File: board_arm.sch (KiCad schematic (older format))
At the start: 153 parts, among them SW1 SW_SPDT, U1 STM32F072CBT6, U2 PRTR5V0U2X, U3 MCP1725-3302E_SN

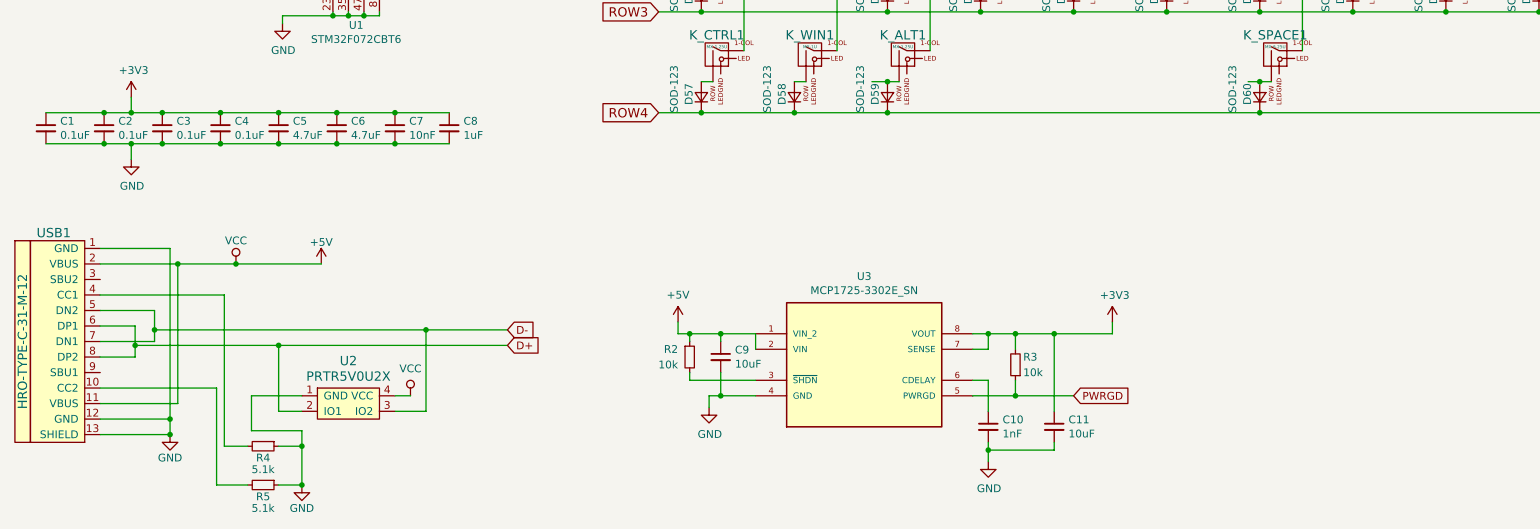
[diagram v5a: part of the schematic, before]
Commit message: basic routing of sigs and power supply
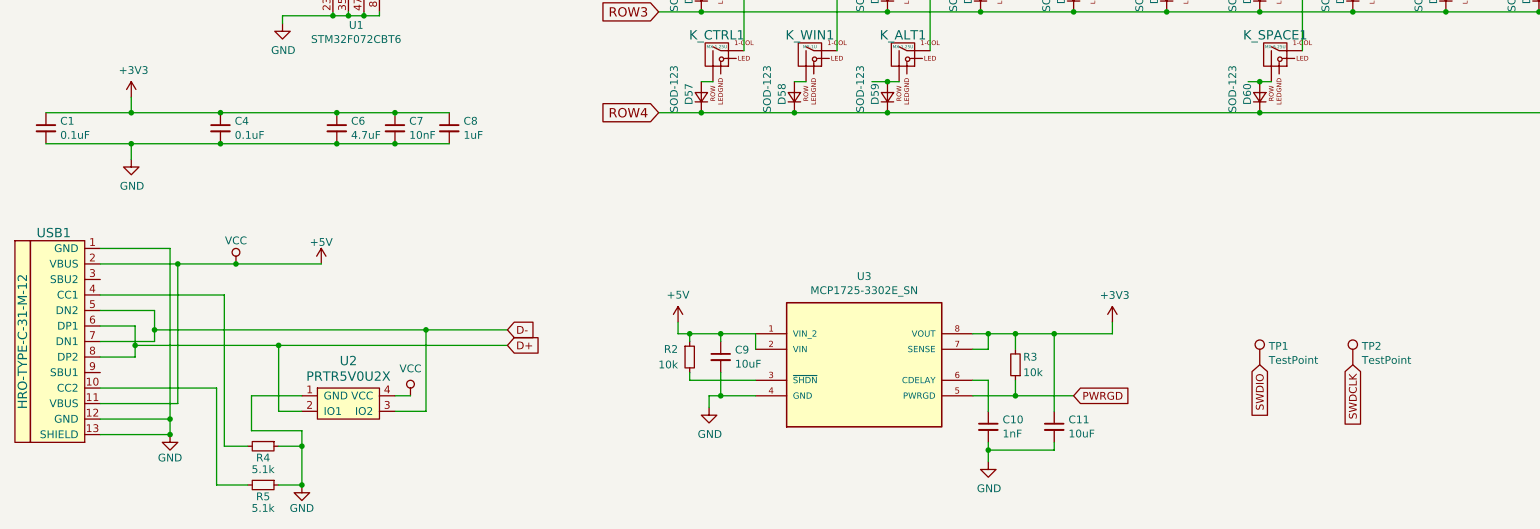
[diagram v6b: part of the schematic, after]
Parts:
- removed C2, C3: 0.1uF, Capacitor_SMD:C_0805_2012Metric, symbol Device:C_Small
- removed C5: 4.7uF, Capacitor_SMD:C_0805_2012Metric, symbol Device:C_Small
- added TP1, TP2: TestPoint, TestPoint:TestPoint_Pad_D1.0mm, symbol Connector:TestPoint
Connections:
- net SWDCLK: now also TP2.1
- net SWDIO: now also TP1.1
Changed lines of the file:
@@
-$EndComp
-$Comp
-L Device:C_Small C2
-U 1 1 5C603F7E
-P 1450 5275
-F 0 "C2" H 1542 5321 50  0000 L CNN
-F 1 "0.1uF" H 1542 5230 50  0000 L CNN
-F 2 "Capacitor_SMD:C_0805_2012Metric" H 1450 5275 50  0001 C CNN
-F 3 "~" H 1450 5275 50  0001 C CNN
-	1    1450 5275
-	1    0    0    -1
-$EndComp
-$Comp
-L Device:C_Small C3
-U 1 1 5C603FAE
-P 1825 5275
-F 0 "C3" H 1917 5321 50  0000 L CNN
-F 1 "0.1uF" H 1917 5230 50  0000 L CNN
-F 2 "Capacitor_SMD:C_0805_2012Metric" H 1825 5275 50  0001 C CNN
-F 3 "~" H 1825 5275 50  0001 C CNN
-	1    1825 5275
-	1    0    0    -1
 $EndComp
 $Comp
@@
 PWRGD
 $Comp
-L Device:C_Small C5
-U 1 1 5D260E0E
-P 2575 5275
-F 0 "C5" H 2667 5321 50  0000 L CNN
-F 1 "4.7uF" H 2667 5230 50  0000 L CNN
-F 2 "Capacitor_SMD:C_0805_2012Metric" H 2575 5275 50  0001 C CNN
-F 3 "~" H 2575 5275 50  0001 C CNN
-	1    2575 5275
-	1    0    0    -1
-$EndComp
-$Comp
 L Device:C_Small C6
 U 1 1 5D2621C9
@@
 Wire Wire Line
 	3325 1500 3500 1500
-Connection ~ 1450 5175
-Connection ~ 1450 5375
-Connection ~ 1825 5175
-Connection ~ 1825 5375
 Connection ~ 2200 5175
 Connection ~ 2200 5375
-Connection ~ 2575 5175
-Connection ~ 2575 5375
 Connection ~ 2950 5175
 Connection ~ 2950 5375
 Wire Wire Line
-	1825 5375 2200 5375
-Wire Wire Line
-	1075 5375 1450 5375
-Wire Wire Line
-	1075 5175 1450 5175
-Wire Wire Line
-	1825 5175 2200 5175
-Wire Wire Line
-	2575 5175 2950 5175
-Wire Wire Line
-	2575 5375 2950 5375
-Wire Wire Line
-	2200 5175 2575 5175
-Wire Wire Line
 	2950 5175 3325 5175
-Wire Wire Line
-	2200 5375 2575 5375
 Connection ~ 3325 5175
 Wire Wire Line
@@
 	1625 5175 1625 5075
 Connection ~ 1625 5175
-Wire Wire Line
-	1625 5175 1825 5175
-Wire Wire Line
-	1450 5175 1625 5175
 Connection ~ 1625 5375
-Wire Wire Line
-	1625 5375 1825 5375
-Wire Wire Line
-	1450 5375 1625 5375
 Wire Wire Line
 	7150 6700 7050 6700
@@
 Wire Wire Line
 	9175 2050 9175 4775
+$Comp
+L Connector:TestPoint TP1
+U 1 1 5C6EFC1B
+P 8900 6800
+F 0 "TP1" H 8958 6920 50  0000 L CNN
+F 1 "TestPoint" H 8958 6829 50  0000 L CNN
+F 2 "TestPoint:TestPoint_Pad_D1.0mm" H 9100 6800 50  0001 C CNN
+F 3 "~" H 9100 6800 50  0001 C CNN
+	1    8900 6800
+	1    0    0    -1
+$EndComp
+Text GLabel 8900 6800 3    50   Input ~ 0
+SWDIO
+Text GLabel 9500 6800 3    50   Input ~ 0
+SWDCLK
+$Comp
+L Connector:TestPoint TP2
+U 1 1 5C7259A1
+P 9500 6800
+F 0 "TP2" H 9558 6920 50  0000 L CNN
+F 1 "TestPoint" H 9558 6829 50  0000 L CNN
+F 2 "TestPoint:TestPoint_Pad_D1.0mm" H 9700 6800 50  0001 C CNN
+F 3 "~" H 9700 6800 50  0001 C CNN
+	1    9500 6800
+	1    0    0    -1
+$EndComp
+Wire Wire Line
+	1075 5175 1625 5175
+Wire Wire Line
+	1075 5375 1625 5375
+Wire Wire Line
+	1625 5175 2200 5175
+Wire Wire Line
+	1625 5375 2200 5375
+Wire Wire Line
+	2200 5175 2950 5175
+Wire Wire Line
+	2200 5375 2950 5375
 $EndSCHEMATC

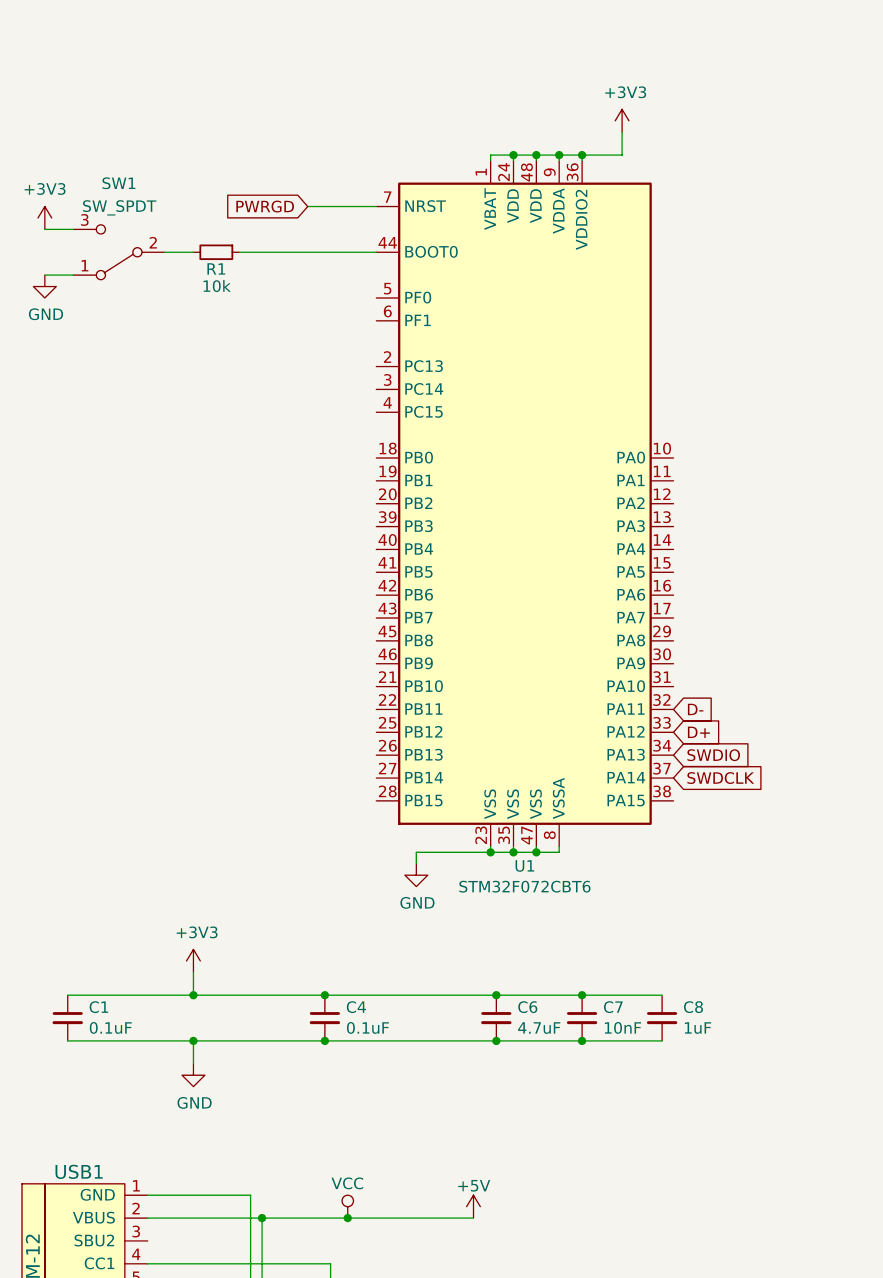
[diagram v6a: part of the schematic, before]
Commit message: correction sur un condo. alim terminée. reste à tirer les signaux ligne et col
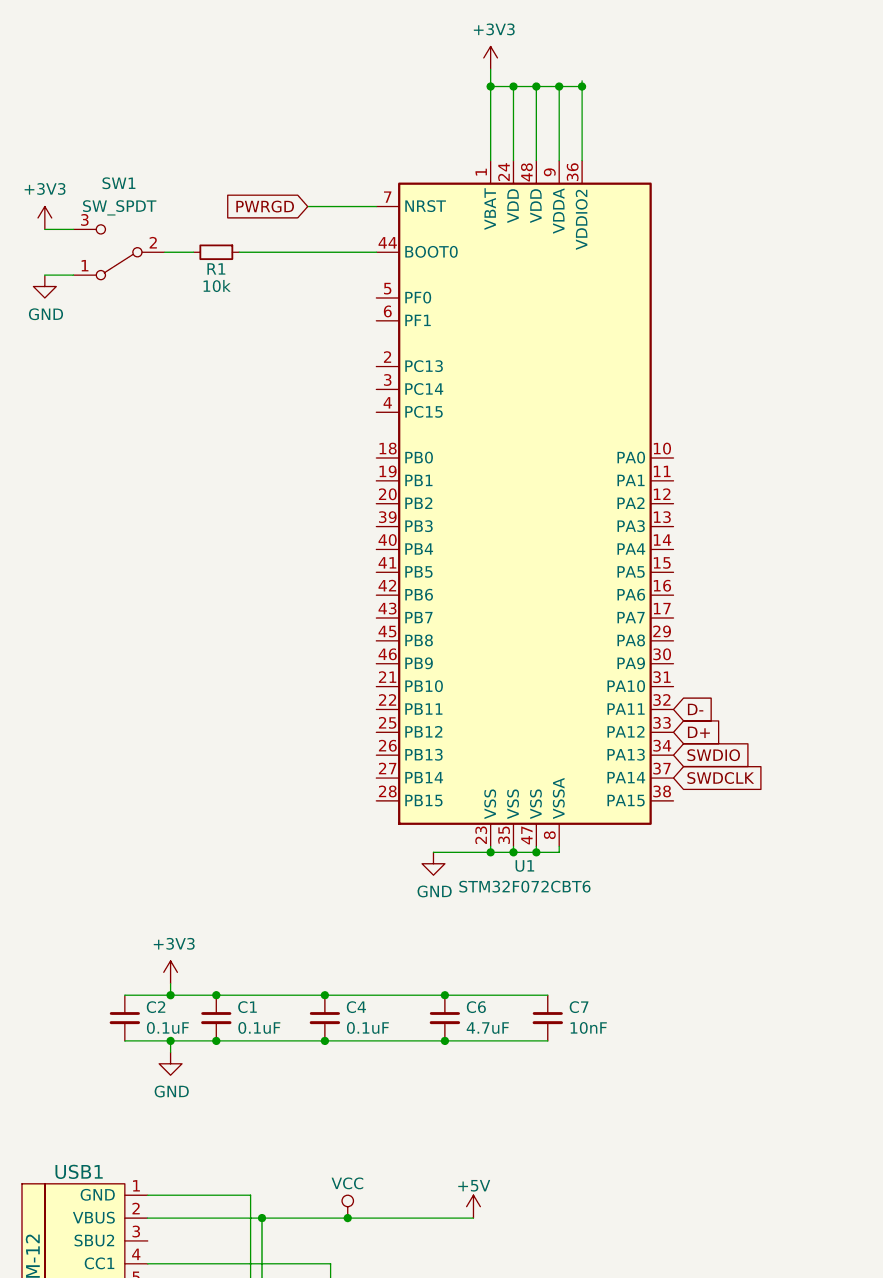
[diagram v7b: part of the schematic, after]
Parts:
- removed C8: 1uF, Capacitor_SMD:C_0805_2012Metric, symbol Device:C_Small
- added C2: 0.1uF, Capacitor_SMD:C_0805_2012Metric, symbol Device:C_Small
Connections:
- net +3V3: now also C2.1
- net GND: now also C2.2
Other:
- moved on the sheet: C1, C6, C7
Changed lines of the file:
@@
 L Device:C_Small C1
 U 1 1 5C603E42
-P 1075 5275
-F 0 "C1" H 1167 5321 50  0000 L CNN
-F 1 "0.1uF" H 1167 5230 50  0000 L CNN
-F 2 "Capacitor_SMD:C_0805_2012Metric" H 1075 5275 50  0001 C CNN
-F 3 "~" H 1075 5275 50  0001 C CNN
-	1    1075 5275
+P 1725 5275
+F 0 "C1" H 1817 5321 50  0000 L CNN
+F 1 "0.1uF" H 1817 5230 50  0000 L CNN
+F 2 "Capacitor_SMD:C_0805_2012Metric" H 1725 5275 50  0001 C CNN
+F 3 "~" H 1725 5275 50  0001 C CNN
+	1    1725 5275
 	1    0    0    -1
 $EndComp
@@
 	1    0    0    -1
 $EndComp
-$Comp
-L power:GND #PWR0105
-U 1 1 5C605AD7
-P 1625 5475
-F 0 "#PWR0105" H 1625 5225 50  0001 C CNN
-F 1 "GND" H 1630 5302 50  0000 C CNN
-F 2 "" H 1625 5475 50  0001 C CNN
-F 3 "" H 1625 5475 50  0001 C CNN
-	1    1625 5475
-	1    0    0    -1
-$EndComp
-Wire Wire Line
-	1625 5475 1625 5375
 $Comp
 L power:+5V #PWR?
@@
 	3525 6575 4050 6575
 $Comp
-L power:+3V3 #PWR0119
-U 1 1 5C7A6D80
-P 3500 1400
-F 0 "#PWR0119" H 3500 1250 50  0001 C CNN
-F 1 "+3V3" H 3515 1573 50  0000 C CNN
-F 2 "" H 3500 1400 50  0001 C CNN
-F 3 "" H 3500 1400 50  0001 C CNN
-	1    3500 1400
-	1    0    0    -1
-$EndComp
-$Comp
-L power:GND #PWR0101
-U 1 1 5C7DAA6D
-P 2600 4600
-F 0 "#PWR0101" H 2600 4350 50  0001 C CNN
-F 1 "GND" H 2605 4427 50  0000 C CNN
-F 2 "" H 2600 4600 50  0001 C CNN
-F 3 "" H 2600 4600 50  0001 C CNN
-	1    2600 4600
-	1    0    0    -1
-$EndComp
-$Comp
 L Switch:SW_SPDT SW?
 U 1 1 5C83E985
@@
 Wire Wire Line
 	975  2025 1100 2025
-$Comp
-L power:+3V3 #PWR0104
-U 1 1 5C9166F9
-P 1625 5075
-F 0 "#PWR0104" H 1625 4925 50  0001 C CNN
-F 1 "+3V3" H 1640 5248 50  0000 C CNN
-F 2 "" H 1625 5075 50  0001 C CNN
-F 3 "" H 1625 5075 50  0001 C CNN
-	1    1625 5075
-	1    0    0    -1
-$EndComp
 Wire Wire Line
 	2300 6150 2850 6150
@@
 L Device:C_Small C6
 U 1 1 5D2621C9
-P 2950 5275
-F 0 "C6" H 3042 5321 50  0000 L CNN
-F 1 "4.7uF" H 3042 5230 50  0000 L CNN
-F 2 "Capacitor_SMD:C_0805_2012Metric" H 2950 5275 50  0001 C CNN
-F 3 "~" H 2950 5275 50  0001 C CNN
-	1    2950 5275
+P 2725 5275
+F 0 "C6" H 2817 5321 50  0000 L CNN
+F 1 "4.7uF" H 2817 5230 50  0000 L CNN
+F 2 "Capacitor_SMD:C_0805_2012Metric" H 2725 5275 50  0001 C CNN
+F 3 "~" H 2725 5275 50  0001 C CNN
+	1    2725 5275
 	1    0    0    -1
 $EndComp
@@
 L Device:C_Small C7
 U 1 1 5D29FD29
-P 3325 5275
-F 0 "C7" H 3417 5321 50  0000 L CNN
-F 1 "10nF" H 3417 5230 50  0000 L CNN
-F 2 "Capacitor_SMD:C_0805_2012Metric" H 3325 5275 50  0001 C CNN
-F 3 "~" H 3325 5275 50  0001 C CNN
-	1    3325 5275
-	1    0    0    -1
-$EndComp
-$Comp
-L Device:C_Small C8
-U 1 1 5D2A0066
-P 3675 5275
-F 0 "C8" H 3767 5321 50  0000 L CNN
-F 1 "1uF" H 3767 5230 50  0000 L CNN
-F 2 "Capacitor_SMD:C_0805_2012Metric" H 3675 5275 50  0001 C CNN
-F 3 "~" H 3675 5275 50  0001 C CNN
-	1    3675 5275
+P 3175 5275
+F 0 "C7" H 3267 5321 50  0000 L CNN
+F 1 "10nF" H 3267 5230 50  0000 L CNN
+F 2 "Capacitor_SMD:C_0805_2012Metric" H 3175 5275 50  0001 C CNN
+F 3 "~" H 3175 5275 50  0001 C CNN
+	1    3175 5275
 	1    0    0    -1
 $EndComp
@@
 	3225 4525 3225 4550
 Wire Wire Line
-	3225 4550 3125 4550
-Wire Wire Line
-	2600 4550 2600 4600
-Wire Wire Line
 	2925 4525 2925 4550
-Connection ~ 2925 4550
-Wire Wire Line
-	2925 4550 2600 4550
 Wire Wire Line
 	3025 4525 3025 4550
@@
 Wire Wire Line
 	3125 4525 3125 4550
-Connection ~ 3125 4550
 Wire Wire Line
 	3125 4550 3025 4550
-Wire Wire Line
-	2925 1525 2925 1500
-Wire Wire Line
-	2925 1500 3025 1500
-Wire Wire Line
-	3500 1500 3500 1400
-Wire Wire Line
-	3025 1525 3025 1500
-Connection ~ 3025 1500
-Wire Wire Line
-	3025 1500 3125 1500
-Wire Wire Line
-	3125 1525 3125 1500
-Connection ~ 3125 1500
-Wire Wire Line
-	3125 1500 3225 1500
-Wire Wire Line
-	3225 1525 3225 1500
-Connection ~ 3225 1500
-Wire Wire Line
-	3225 1500 3325 1500
-Wire Wire Line
-	3325 1525 3325 1500
-Connection ~ 3325 1500
-Wire Wire Line
-	3325 1500 3500 1500
-Connection ~ 2200 5175
-Connection ~ 2200 5375
-Connection ~ 2950 5175
-Connection ~ 2950 5375
-Wire Wire Line
-	2950 5175 3325 5175
-Connection ~ 3325 5175
-Wire Wire Line
-	3325 5175 3675 5175
-Wire Wire Line
-	2950 5375 3325 5375
-Connection ~ 3325 5375
-Wire Wire Line
-	3325 5375 3675 5375
-Wire Wire Line
-	1625 5175 1625 5075
-Connection ~ 1625 5175
-Connection ~ 1625 5375
 Wire Wire Line
 	7150 6700 7050 6700
@@
 $EndComp
 Wire Wire Line
-	1075 5175 1625 5175
-Wire Wire Line
-	1075 5375 1625 5375
-Wire Wire Line
-	1625 5175 2200 5175
-Wire Wire Line
-	1625 5375 2200 5375
-Wire Wire Line
-	2200 5175 2950 5175
-Wire Wire Line
-	2200 5375 2950 5375
+	2200 5175 1725 5175
+Connection ~ 2200 5175
+Wire Wire Line
+	1725 5375 2200 5375
+Connection ~ 2200 5375
+Wire Wire Line
+	2925 1125 2925 1200
+$Comp
+L power:+3V3 #PWR0101
+U 1 1 5CC8408D
+P 2925 1125
+F 0 "#PWR0101" H 2925 975 50  0001 C CNN
+F 1 "+3V3" H 2940 1298 50  0000 C CNN
+F 2 "" H 2925 1125 50  0001 C CNN
+F 3 "" H 2925 1125 50  0001 C CNN
+	1    2925 1125
+	1    0    0    -1
+$EndComp
+Wire Wire Line
+	2675 4550 2925 4550
+Connection ~ 2925 4550
+$Comp
+L Device:C_Small C2
+U 1 1 5CD1A706
+P 1325 5275
+F 0 "C2" H 1417 5321 50  0000 L CNN
+F 1 "0.1uF" H 1417 5230 50  0000 L CNN
+F 2 "Capacitor_SMD:C_0805_2012Metric" H 1325 5275 50  0001 C CNN
+F 3 "~" H 1325 5275 50  0001 C CNN
+	1    1325 5275
+	1    0    0    -1
+$EndComp
+Wire Wire Line
+	1325 5175 1525 5175
+Connection ~ 1725 5175
+Wire Wire Line
+	1325 5375 1525 5375
+Connection ~ 1725 5375
+Wire Wire Line
+	3025 1200 3125 1200
+Wire Wire Line
+	3325 1200 3325 1525
+Wire Wire Line
+	3025 1200 3025 1525
+Wire Wire Line
+	3125 1525 3125 1200
+Connection ~ 3125 1200
+Wire Wire Line
+	3125 1200 3225 1200
+Wire Wire Line
+	3325 1200 3325 1175
+Connection ~ 3325 1200
+$Comp
+L power:+3V3 #PWR0104
+U 1 1 5CE76AF3
+P 1525 5125
+F 0 "#PWR0104" H 1525 4975 50  0001 C CNN
+F 1 "+3V3" H 1540 5298 50  0000 C CNN
+F 2 "" H 1525 5125 50  0001 C CNN
+F 3 "" H 1525 5125 50  0001 C CNN
+	1    1525 5125
+	1    0    0    -1
+$EndComp
+$Comp
+L power:GND #PWR0105
+U 1 1 5CE8CFE7
+P 1525 5425
+F 0 "#PWR0105" H 1525 5175 50  0001 C CNN
+F 1 "GND" H 1530 5252 50  0000 C CNN
+F 2 "" H 1525 5425 50  0001 C CNN
+F 3 "" H 1525 5425 50  0001 C CNN
+	1    1525 5425
+	1    0    0    -1
+$EndComp
+Wire Wire Line
+	1525 5125 1525 5175
+Connection ~ 1525 5175
+Wire Wire Line
+	1525 5175 1725 5175
+Wire Wire Line
+	1525 5425 1525 5375
+Connection ~ 1525 5375
+Wire Wire Line
+	1525 5375 1725 5375
+Wire Wire Line
+	2200 5375 2725 5375
+Wire Wire Line
+	2200 5175 2725 5175
+Wire Wire Line
+	2725 5175 3175 5175
+Connection ~ 2725 5175
+Wire Wire Line
+	3175 5375 2725 5375
+Connection ~ 2725 5375
+Wire Wire Line
+	3225 4550 3125 4550
+Connection ~ 3125 4550
+Wire Wire Line
+	3225 1525 3225 1200
+Connection ~ 3225 1200
+Wire Wire Line
+	3225 1200 3325 1200
+Wire Wire Line
+	2925 1200 3025 1200
+Connection ~ 2925 1200
+Wire Wire Line
+	2925 1200 2925 1525
+Connection ~ 3025 1200
+$Comp
+L power:GND #PWR?
+U 1 1 5D08B550
+P 2675 4550
+F 0 "#PWR?" H 2675 4300 50  0001 C CNN
+F 1 "GND" H 2680 4377 50  0000 C CNN
+F 2 "" H 2675 4550 50  0001 C CNN
+F 3 "" H 2675 4550 50  0001 C CNN
+	1    2675 4550
+	1    0    0    -1
+$EndComp
 $EndSCHEMATC
